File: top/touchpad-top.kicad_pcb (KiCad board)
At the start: 2 copper layers, 28.3 x 40 mm, 19 parts, among them P1 CONN_10, P2 CONN_5, U1 IQS572, U4 ESD

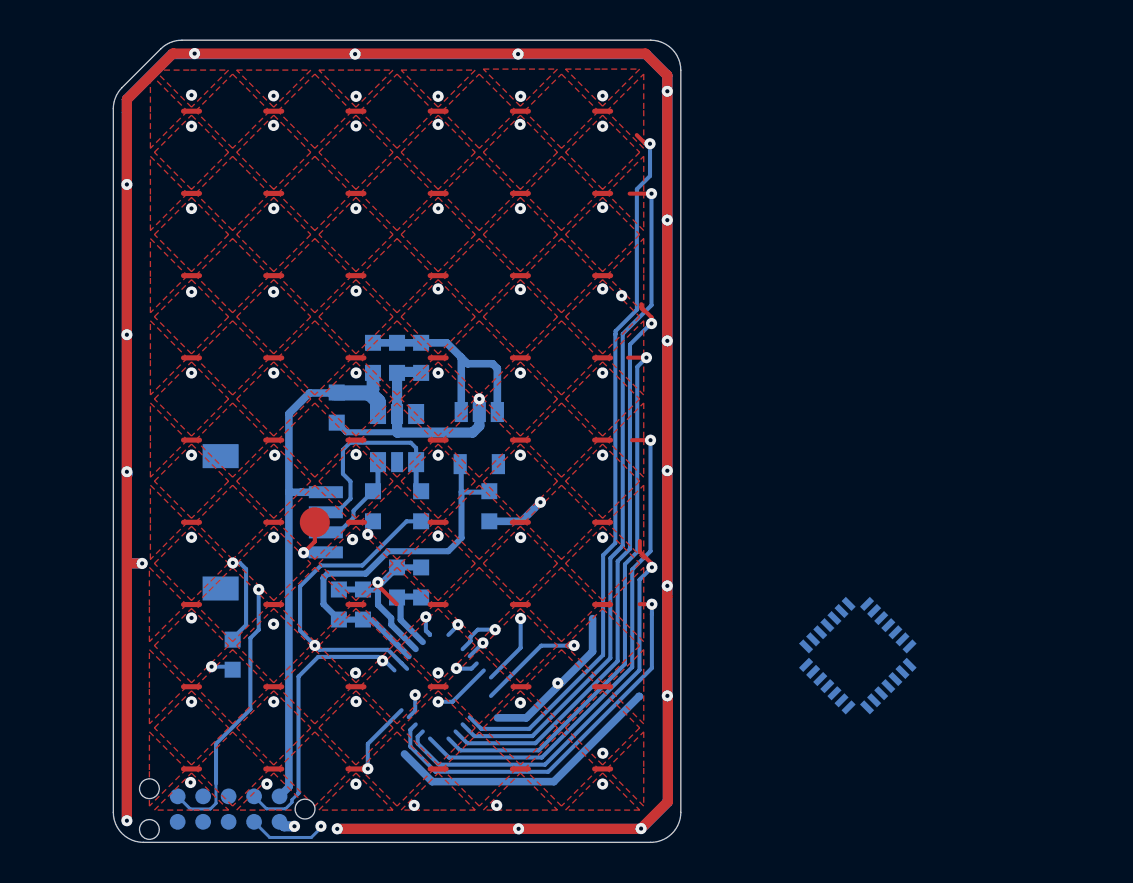
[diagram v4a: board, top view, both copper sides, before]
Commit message: Arrange components outside of pcb.
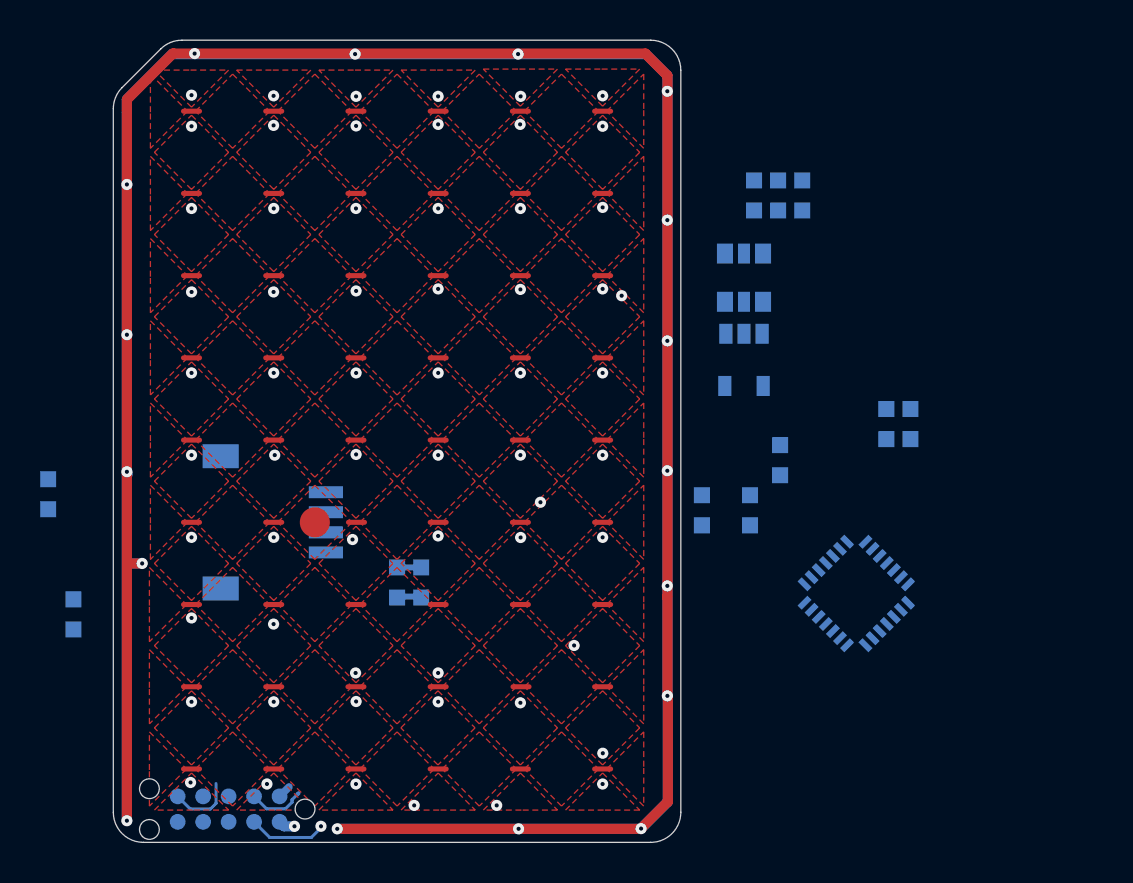
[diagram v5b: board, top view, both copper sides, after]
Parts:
- moved C5 28.7 mm to (231.3, 137.6)
- moved C6 28.7 mm to (230.1, 137.6)
- moved C2 20.7 mm to (224.7, 126.2)
- moved C8 20.7 mm to (225.9, 126.2)
- moved FB2 20.7 mm to (223.5, 126.2)
- moved U4 19.1 mm to (223.0, 130.3)
- moved R6 16.4 mm to (223.3, 141.9)
- moved R7 16.4 mm to (220.9, 141.9)
- moved C7 15.0 mm to (188.3, 141.1)
- moved C12 14.7 mm to (224.8, 139.4)
- moved VR1 13.8 mm to (223.0, 134.4)
- moved C1 8.19 mm to (189.6, 147.1)
- moved U1 3.10 mm to (228.6, 146.1), turned to 135 degrees
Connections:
- P1 pad 5: (no net) -> Net-(P1-Pad5)
- P1 pad 6: (no net) -> Net-(P1-Pad6)
- P1 pad 7: (no net) -> Net-(P1-Pad7)
- P1 pad 8: (no net) -> Net-(P1-Pad8)
- P1 pad 9: (no net) -> Net-(P1-Pad9)
- U1 pad 1: (no net) -> Net-(U1-Pad1)
- U1 pad 16: (no net) -> Net-(U1-Pad16)
- U1 pad 17: (no net) -> Net-(U1-Pad17)
- U1 pad 27: (no net) -> /PGM
- U1 pad 28: (no net) -> Net-(U1-Pad28)
- U1 pad 9: (no net) -> Net-(U1-Pad9)
- VR1 pad 4: (no net) -> Net-(VR1-Pad4)
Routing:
- net GND: track 290.3 -> 238.8 mm, vias 25 -> 20
- net /TX0: track 40.5 -> 4.80 mm, vias 1 -> 0
- net /TX1: track 39.1 -> 4.80 mm, vias 1 -> 0
- net /TX2: track 33.6 -> 4.80 mm, vias 1 -> 0
- net /TX3: track 32.3 -> 4.80 mm, vias 1 -> 0
- net /VCC_BOTTOM: track 27.9 -> 0.66 mm
- net /TX4: track 29.8 -> 4.80 mm, vias 1 -> 0
- net /TX5: track 26.0 -> 4.80 mm, vias 1 -> 0
- net /TX6: track 24.5 -> 4.80 mm, vias 1 -> 0
- net +3V3: track 18.8 -> 0.00 mm
- net /SCL: track 19.7 -> 3.93 mm, vias 2 -> 1
- net /SDA: track 15.0 -> 2.87 mm, vias 2 -> 0
- net +5V: track 11.7 -> 0.00 mm
- net /RDY: track 14.5 -> 3.28 mm, vias 2 -> 0
- net /SCL_BOTTOM: track 9.43 -> 0.00 mm
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- added copper zone on F.Cu, net (none)

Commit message: Add RX and TX paths.
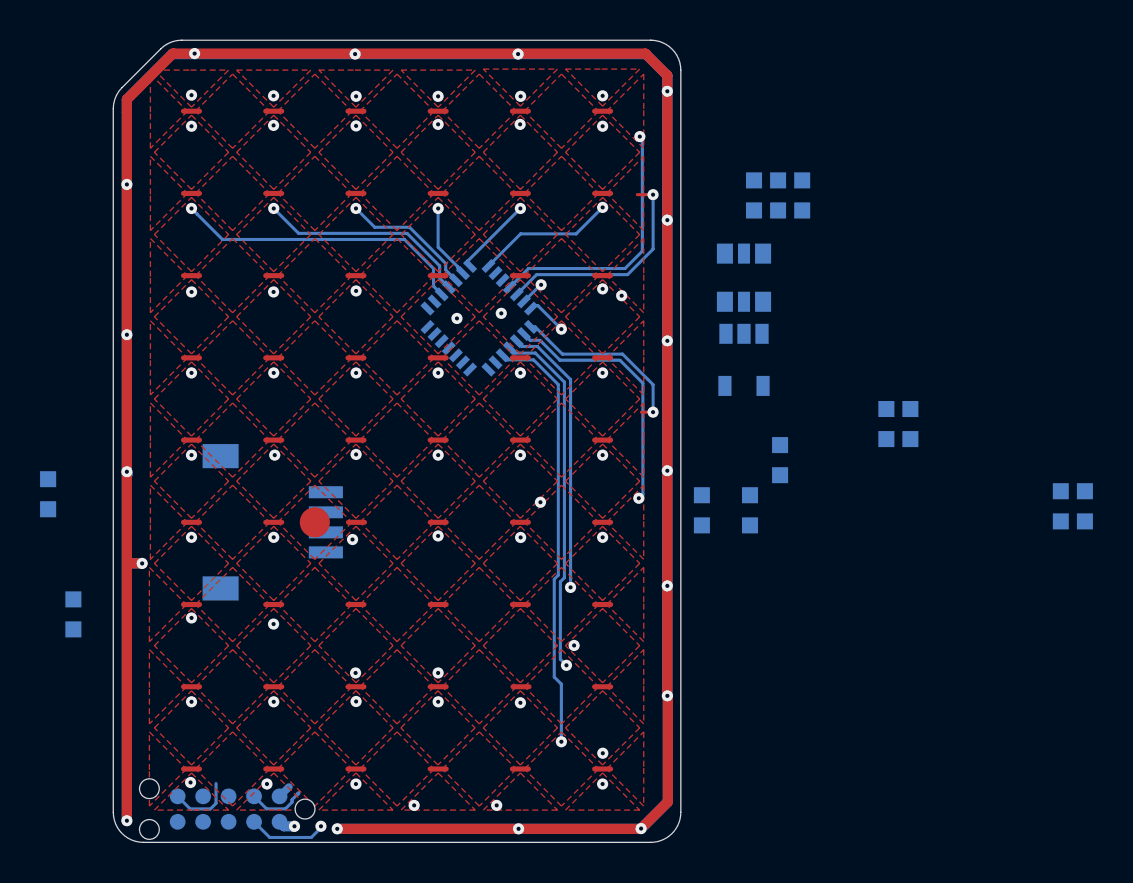
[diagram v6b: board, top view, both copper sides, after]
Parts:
- moved C4 33.3 mm to (238.8, 141.7)
- moved C3 33.3 mm to (240.0, 141.7)
- moved U1 23.3 mm to (209.8, 132.3), turned to 45 degrees
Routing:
- net /TX8: track 4.80 -> 26.2 mm, vias 0 -> 1
- net /TX7: track 4.80 -> 22.6 mm, vias 0 -> 1
- net /RX0: track 0.00 -> 14.9 mm
- net /TX6: track 4.80 -> 18.6 mm, vias 0 -> 1
- net /TX0: track 4.80 -> 17.9 mm, vias 0 -> 1
- net /TX5: track 4.80 -> 17.6 mm, vias 0 -> 1
- net /TX1: track 4.80 -> 16.0 mm, vias 0 -> 1
- net /RX1: track 0.00 -> 10.7 mm
- net /TX4: track 4.80 -> 14.0 mm, vias 0 -> 1
- net /RX5: track 0.02 -> 6.92 mm
- net /RX2: track 0.00 -> 6.66 mm
- net /RX4: track 0.00 -> 4.03 mm
- net /RX3: track 0.00 -> 3.73 mm
- net /TX3: track 4.80 -> 6.85 mm, vias 0 -> 1
- net Net-(C3-Pad2): track 1.43 -> 0.00 mm
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
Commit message: Temporarí commit.
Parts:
- removed C2: 1uF, UGL:SM0603
- removed C8: 0.1uF, UGL:SM0603
- removed hole: 1.5mm, UGL:smd_pad_1.5mm
- moved C3 36.5 mm to (204.5, 133.1), turned to 45 degrees
- moved C4 34.3 mm to (205.4, 134.0), turned to 45 degrees
- moved C5 25.2 mm to (206.2, 134.8), turned to 45 degrees
- moved C6 23.1 mm to (207.1, 135.6), turned to 45 degrees
- moved C1 22.4 mm to (205.4, 131.2), turned to 315 degrees
- moved FB2 21.8 mm to (205.8, 138.9), turned to 0 degrees
- moved U4 20.5 mm to (205.8, 141.5)
- moved R6 16.8 mm to (206.8, 144.8)
- moved R7 16.4 mm to (204.8, 144.8)
- moved C12 15.2 mm to (209.7, 137.6), turned to 0 degrees
- moved VR1 14.5 mm to (209.7, 140.2), turned to 0 degrees
- moved C7 14.4 mm to (202.6, 139.1), turned to 270 degrees
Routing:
- net GND: track 237.6 -> 255.7 mm, vias 20 -> 17
- net /RX2: track 6.66 -> 21.0 mm, vias 10 -> 18
- net /RX1: track 10.7 -> 24.4 mm, vias 10 -> 18
- net /RX0: track 14.9 -> 28.5 mm, vias 10 -> 18
- net /RX5: track 6.92 -> 18.8 mm, vias 10 -> 14
- net /RX3: track 3.73 -> 14.1 mm, vias 10 -> 15
- net /RX4: track 4.03 -> 14.3 mm, vias 9 -> 16
- net /SCL: track 3.93 -> 0.00 mm, vias 1 -> 0
- net /TX2: track 6.03 -> 6.74 mm, vias 1 -> 3
- net /TX3: track 6.85 -> 7.35 mm, vias 1 -> 3
- removed copper zone on F.Cu, net (none)

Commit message: End of day commit.
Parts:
- moved U1 2.94 mm to (211.8, 130.2)
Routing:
- net /RX0: track 28.5 -> 14.8 mm, vias 18 -> 1
- net /RX5: track 18.8 -> 5.72 mm, vias 14 -> 1
- net /RX1: track 24.4 -> 12.7 mm, vias 18 -> 1
- net /RX4: track 14.3 -> 3.43 mm, vias 16 -> 1
- net /RX2: track 21.0 -> 10.2 mm, vias 18 -> 1
- net GND: track 255.7 -> 247.0 mm, vias 17 -> 19
- net /RX3: track 14.1 -> 6.16 mm, vias 15 -> 1
- net /TX3: track 7.35 -> 2.05 mm, vias 3 -> 2
- net /TX5: track 17.6 -> 13.7 mm
- net /TX6: track 18.6 -> 22.2 mm, vias 1 -> 12
- net /TX7: track 22.6 -> 25.9 mm, vias 1 -> 13
- net /TX8: track 26.2 -> 29.4 mm, vias 1 -> 13
- net (no net): track 0.00 -> 2.49 mm, vias 0 -> 6
- net /TX0: track 17.9 -> 19.3 mm, vias 1 -> 13
- net /SDA_BOTTOM: track 0.92 -> 0.00 mm
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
